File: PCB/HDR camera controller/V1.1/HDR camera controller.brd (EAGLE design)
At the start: 58 x 48 mm, 63 parts, among them IC1 USBLC6-4, IC10 RS422-SO8, IC11 RS422-SO8, IC12 USBLC6-4, IC14 741G157, IC2 RS422-SO8, IC3 RS422-SO8, IC4 RS422-SO8, IC6 FT232RL, IC7 74HC00D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

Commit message: wip
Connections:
- net ENC_B: now also IC13.2; no longer IC13.27
- net LINE_IN_1: now also IC13.13; no longer IC13.10
- net L_IN: now also IC13.14; no longer IC13.9
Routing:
- net LINE_IN_1: track 35.5 -> 34.4 mm
- net ENC_B: track 94.1 -> 93.3 mm
- net L_IN: track 33.1 -> 32.5 mm
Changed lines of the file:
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@@
 </layers>
 <board>
-<fusionsync huburn="a.cGVyc29uYWw6dWUyYWFhMjdi" projecturn="a.cGVyc29uYWw6dWUyYWFhMjdiIzIwMTcxMTIzMTA1NDAxMzMx" f3durn="urn:adsk.wipprod:dm.lineage:Xuph5AAnRz6wK6HHSwnN2A" pcbguid="" lastpulledtime="" lastsyncedchangeguid="" latestrevisionid="6616cd26-1267-4b75-a275-6117032d61cd" lastsyncedrevisionid="6616cd26-1267-4b75-a275-6117032d61cd" lastboardhashguid="059826bd-0402-169d-34a1-e7c392c3920d" lastpushedtime="2021-12-01T15:11:12Z" linktopcb3d="true"/>
+<fusionsync huburn="a.cGVyc29uYWw6dWUyYWFhMjdi" projecturn="a.cGVyc29uYWw6dWUyYWFhMjdiIzIwMTcxMTIzMTA1NDAxMzMx" f3durn="urn:adsk.wipprod:dm.lineage:Xuph5AAnRz6wK6HHSwnN2A" pcbguid="" lastpulledtime="" lastsyncedchangeguid="" latestrevisionid="6616cd26-1267-4b75-a275-6117032d61cd" lastsyncedrevisionid="6616cd26-1267-4b75-a275-6117032d61cd" lastboardhashguid="059826bd-0402-169d-34a1-e7c392c3920d" lastpushedtime="2021-12-01T15:11:12Z" linktopcb3d="false"/>
 <plain>
 <wire x1="0" y1="44.5" x2="0" y2="3.5" width="0" layer="20"/>
@@
 <contactref element="IC2" pad="3"/>
 <contactref element="R2" pad="2"/>
-<contactref element="IC13" pad="10"/>
 <wire x1="17.0434" y1="6.985" x2="20.32" y2="6.985" width="0.4064" layer="1"/>
 <wire x1="20.32" y1="6.985" x2="20.955" y2="6.985" width="0.4064" layer="1"/>
@@
 <wire x1="24.13" y1="6.35" x2="21.59" y2="6.35" width="0.4064" layer="1"/>
 <wire x1="21.59" y1="6.35" x2="20.955" y2="6.985" width="0.4064" layer="1"/>
-<wire x1="32.29" y1="18.5674" x2="32.29" y2="17.494" width="0.4064" layer="1"/>
 <wire x1="36.83" y1="16.51" x2="36.068" y2="17.272" width="0.4064" layer="1"/>
 <wire x1="36.068" y1="17.272" x2="32.512" y2="17.272" width="0.4064" layer="1"/>
@@
 <wire x1="32.29" y1="17.494" x2="32.512" y2="17.272" width="0.4064" layer="1"/>
 <wire x1="36.83" y1="8.89" x2="33.909" y2="5.969" width="0.4064" layer="16"/>
+<contactref element="IC13" pad="13"/>
+<wire x1="32.29" y1="17.494" x2="34.69" y2="18.5674" width="0" layer="19" extent="1-1"/>
 </signal>
 <signal name="LINE_OUT_1">
@@
 <contactref element="IC7" pad="12"/>
 <contactref element="R7" pad="2"/>
-<contactref element="IC13" pad="9"/>
 <wire x1="26.67" y1="38.8366" x2="27.94" y2="38.8366" width="0.4064" layer="1"/>
 <wire x1="27.94" y1="40.259" x2="27.94" y2="38.8366" width="0.4064" layer="1"/>
@@
 <wire x1="29.21" y1="41.529" x2="29.21" y2="36.83" width="0.4064" layer="16"/>
 <wire x1="29.21" y1="36.83" x2="28.067" y2="35.687" width="0.4064" layer="16"/>
-<wire x1="31.49" y1="18.5674" x2="30.8356" y2="18.5674" width="0.4064" layer="1"/>
 <wire x1="30.8356" y1="18.5674" x2="30.48" y2="18.923" width="0.4064" layer="1"/>
 <via x="30.48" y="18.923" extent="1-16" drill="0.6"/>
 <wire x1="30.48" y1="18.923" x2="29.21" y2="20.193" width="0.4064" layer="16"/>
 <wire x1="29.21" y1="20.193" x2="29.21" y2="29.21" width="0.4064" layer="16"/>
+<contactref element="IC13" pad="14"/>
+<wire x1="30.8356" y1="18.5674" x2="35.49" y2="18.5674" width="0" layer="19" extent="1-1"/>
 </signal>
 <signal name="L_SEL0">
@@
 <contactref element="TRIG" pad="3"/>
 <contactref element="IC4" pad="3"/>
-<contactref element="IC13" pad="27"/>
 <wire x1="2.54" y1="34.29" x2="8.89" y2="34.29" width="0.4064" layer="1"/>
 <via x="8.89" y="34.29" extent="1-16" drill="0.6"/>
@@
 <wire x1="35.56" y1="11.176" x2="35.2298" y2="10.8458" width="0.4064" layer="1"/>
 <wire x1="35.2298" y1="10.8458" x2="34.29" y2="10.8458" width="0.4064" layer="1"/>
-<wire x1="35.49" y1="27.1526" x2="35.49" y2="26.346" width="0.4064" layer="1"/>
 <via x="34.163" y="25.019" extent="1-16" drill="0.6"/>
 <wire x1="34.163" y1="25.019" x2="33.909" y2="24.765" width="0.4064" layer="16"/>
-<wire x1="35.49" y1="26.346" x2="34.163" y2="25.019" width="0.4064" layer="1"/>
+<wire x1="35.49" y1="26.346" x2="34.417" y2="25.273" width="0.4064" layer="1"/>
+<wire x1="34.417" y1="25.273" x2="34.163" y2="25.019" width="0.4064" layer="1"/>
 <wire x1="33.909" y1="24.765" x2="33.909" y2="18.161" width="0.4064" layer="16"/>
 <wire x1="34.3535" y1="17.7165" x2="33.909" y2="18.161" width="0.4064" layer="16"/>
@@
 <via x="22.225" y="11.43" extent="1-16" drill="0.6"/>
 <wire x1="19.05" y1="14.605" x2="22.225" y2="11.43" width="0.4064" layer="1"/>
+<contactref element="IC13" pad="2"/>
+<wire x1="34.417" y1="25.273" x2="29.9974" y2="24.86" width="0" layer="19" extent="1-1"/>
 </signal>
 <signal name="ENC_A">

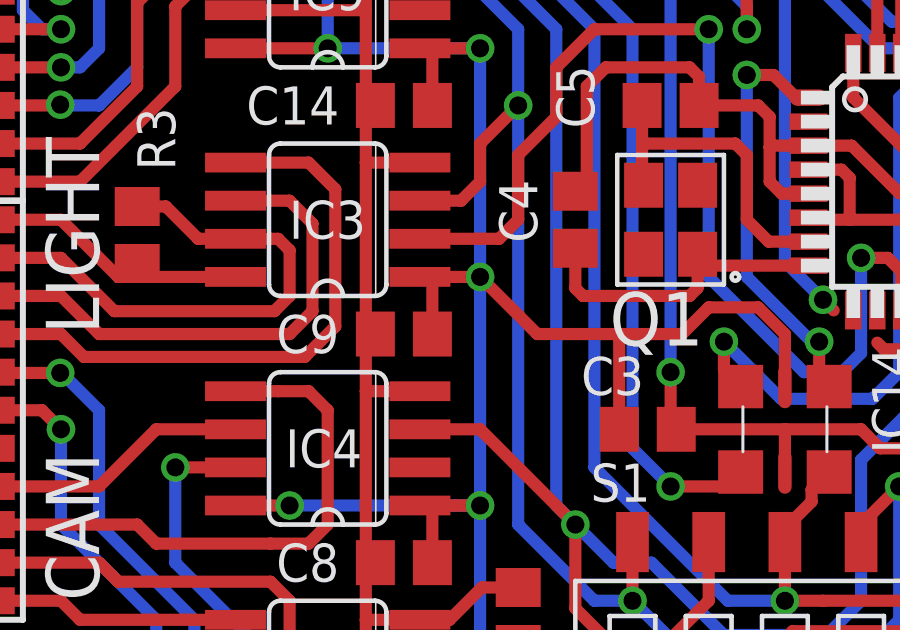
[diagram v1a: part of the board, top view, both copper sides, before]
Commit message: Line in 2 activation during 1st exposure
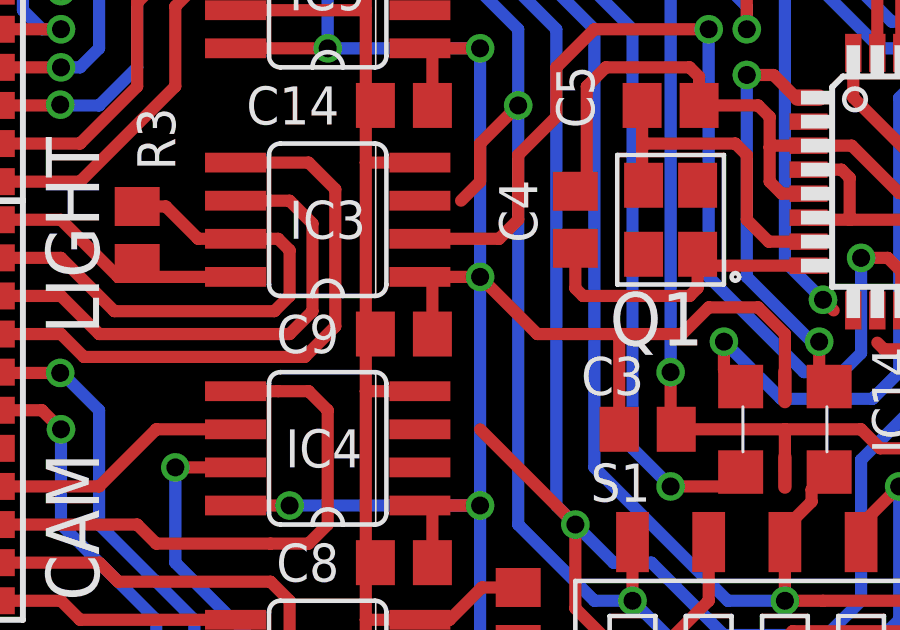
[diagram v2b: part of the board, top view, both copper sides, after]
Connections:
- new net LINE_IN_2: IC13.28, IC3.3
- new net LINE_IN_3: IC4.3
- net ENC_A: no longer IC3.3
- net ENC_B: no longer IC4.3
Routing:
- net ENC_B: track 93.3 -> 91.3 mm
- net ENC_A: track 83.6 -> 82.3 mm
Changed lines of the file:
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@@
 <contactref element="S1" pad="5"/>
 <contactref element="TRIG" pad="3"/>
-<contactref element="IC4" pad="3"/>
 <wire x1="2.54" y1="34.29" x2="8.89" y2="34.29" width="0.4064" layer="1"/>
 <via x="8.89" y="34.29" extent="1-16" drill="0.6"/>
-<wire x1="17.0434" y1="14.605" x2="19.05" y2="14.605" width="0.4064" layer="1"/>
 <wire x1="15.24" y1="34.29" x2="21.59" y2="27.94" width="0.4064" layer="16"/>
 <wire x1="8.89" y1="34.29" x2="15.24" y2="34.29" width="0.4064" layer="16"/>
@@
 <wire x1="19.05" y1="14.605" x2="22.225" y2="11.43" width="0.4064" layer="1"/>
 <contactref element="IC13" pad="2"/>
-<wire x1="34.417" y1="25.273" x2="29.9974" y2="24.86" width="0" layer="19" extent="1-1"/>
+<wire x1="34.163" y1="25.019" x2="29.9974" y2="24.86" width="0" layer="19" extent="1-1"/>
 </signal>
 <signal name="ENC_A">
@@
 <contactref element="S1" pad="6"/>
 <contactref element="TRIG" pad="2"/>
-<contactref element="IC3" pad="3"/>
 <contactref element="IC13" pad="26"/>
 <wire x1="2.54" y1="33.02" x2="8.89" y2="33.02" width="0.4064" layer="1"/>
@@
 <wire x1="33.02" y1="8.255" x2="33.02" y2="12.7" width="0.4064" layer="16"/>
 <wire x1="31.623" y1="6.858" x2="33.02" y2="8.255" width="0.4064" layer="16"/>
-<wire x1="17.0434" y1="22.225" x2="18.415" y2="22.225" width="0.4064" layer="1"/>
 <via x="20.32" y="25.4" extent="1-16" drill="0.6"/>
 <wire x1="18.415" y1="22.225" x2="19.05" y2="22.86" width="0.4064" layer="1"/>
@@
 <wire x1="40.598" y1="22.46" x2="40.96" y2="22.098" width="0.4064" layer="1"/>
 </signal>
+<signal name="LINE_IN_2">
+<contactref element="IC13" pad="28"/>
+<contactref element="IC3" pad="3"/>
+<wire x1="17.0434" y1="22.225" x2="34.69" y2="27.1526" width="0" layer="19" extent="1-1"/>
+</signal>
+<signal name="LINE_IN_3">
+<contactref element="IC4" pad="3"/>
+</signal>
 </signals>

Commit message: Documentation
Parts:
- added R6: 10K, rcl:R0805
- moved IC14 1.17 mm to (28.1, 14.9)
- moved C3 1.14 mm to (23.5, 14.6), turned to 270 degrees
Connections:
- net GND: now also R6.1
- net LINE_IN_3: now also R6.2
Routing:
- net LINE_IN_2: track 0.00 -> 41.1 mm, vias 0 -> 2
- net LINE_OUT_2: track 35.7 -> 20.2 mm, vias 2 -> 0
- net ENC_B: track 91.3 -> 84.9 mm, vias 4 -> 5
- net LINE_OUT_1: track 46.6 -> 51.6 mm
- net ENC_A: track 82.3 -> 77.3 mm, vias 5 -> 4
- net L_IN: track 32.5 -> 36.5 mm
- net GND: track 498.5 -> 494.5 mm, vias 15 -> 14
- net LINE_IN_3: track 0.00 -> 3.67 mm
- net +5V: track 297.5 -> 294.3 mm
- net HW_TRIG_SEL: track 25.9 -> 24.8 mm
- net LINE_IN_1: track 34.4 -> 33.4 mm
- net HW_TRIG: track 14.0 -> 13.2 mm
- net HW_TRIG_RS: track 41.5 -> 40.7 mm
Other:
- board text added: "HDR line cam controller V1.1"
- board text removed: "HDR line cam controller V1"
